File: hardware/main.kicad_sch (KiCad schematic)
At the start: 18 parts, among them J4 ScrewTerminal, J5 ScrewTerminal, J6 ScrewTerminal, K2 ADW11

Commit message: added options
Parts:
- R1, R2: value 3k 100W -> 2k7 50W
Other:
- note added: "Capacitor value: 300 uF Initial charge voltage: 588 V Safety threshold voltage: 60 V Resistance value: 5400 R Safety Voltage achieved by: 3.6975 s Initial power across resistors: 64.0267 W Time constant: 1.62 s Energy discharged to Zero volts: 51.8616 J"
- note removed: "Capacitor value: 300 uF Initial charge voltage: 588 V Safety threshold voltage: 60 V Resistance value: 6000 R Safety Voltage achieved by: 4.10828 s Initial power across resistor: 57.624 W Time constant: 1.8 s Energy discharged to Zero volts: 51.8616 J"

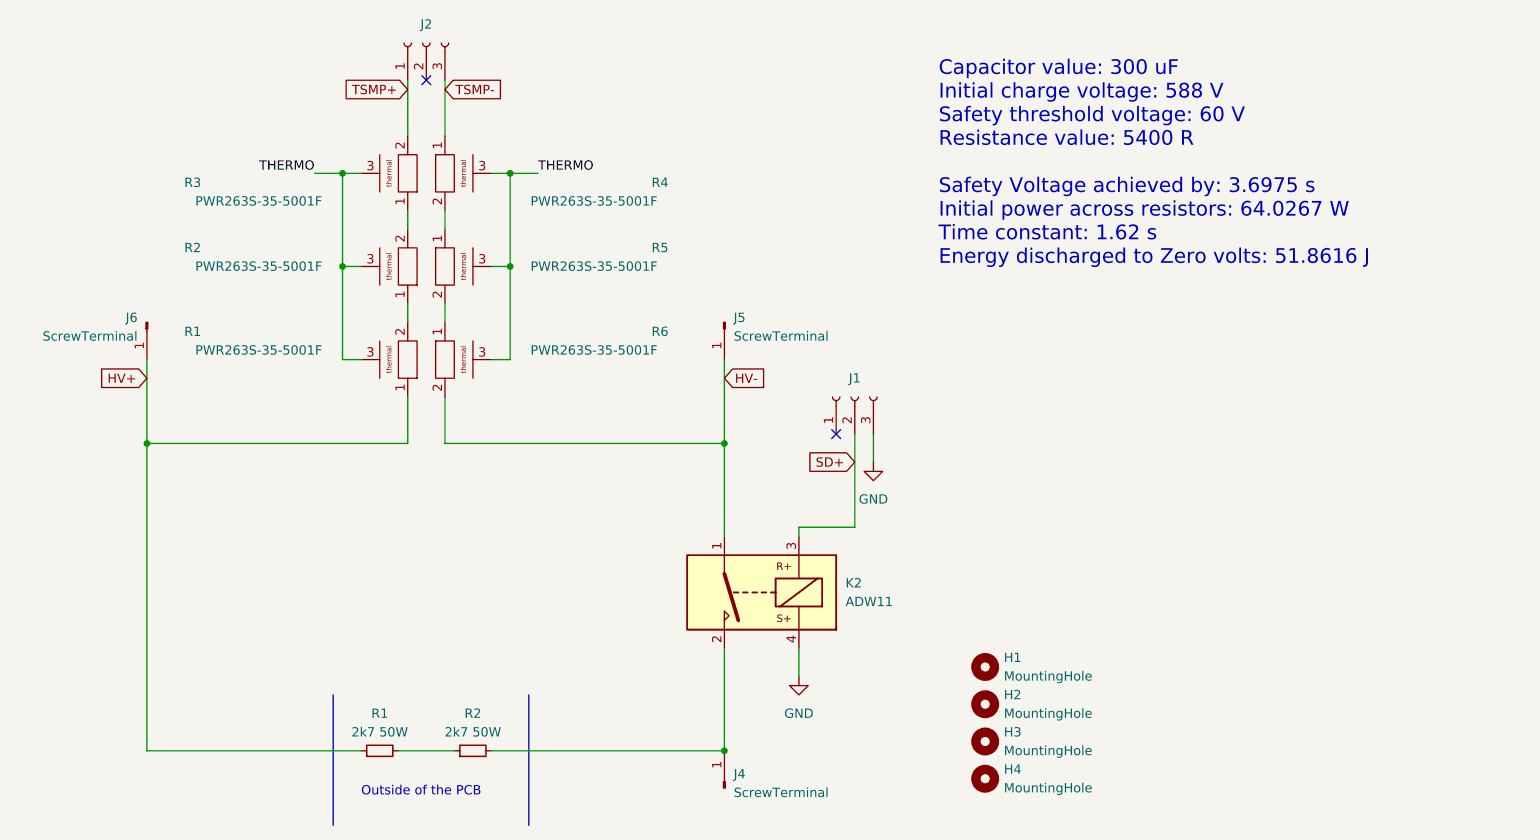
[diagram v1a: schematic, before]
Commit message: Changed resistors to 3x 2k 50W
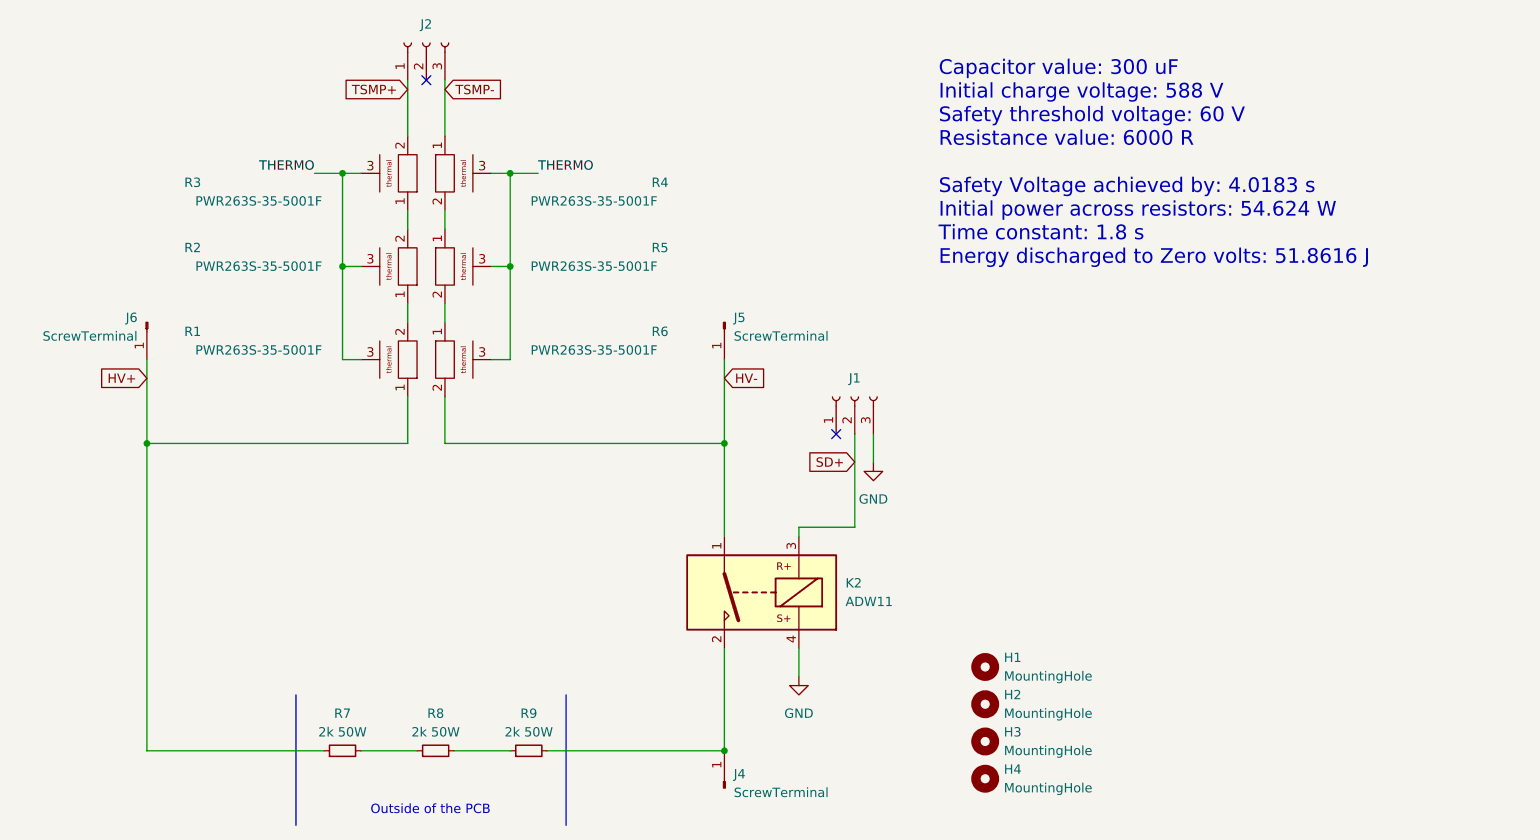
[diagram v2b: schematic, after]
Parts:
- removed R1, R2: 2k7 50W, symbol Device:R_Small
- added R7, R8, R9: 2k 50W, symbol Device:R_Small
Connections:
- net HV+: now also R7.1
- net at J4.1 (Pin_1), K2.2: now also R9.2
- new net: R7.2, R8.1
- new net: R8.2, R9.1
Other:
- note added: "Capacitor value: 300 uF Initial charge voltage: 588 V Safety threshold voltage: 60 V Resistance value: 6000 R Safety Voltage achieved by: 4.0183 s Initial power across resistors: 54.624 W Time constant: 1.8 s Energy discharged to Zero volts: 51.8616 J"
- note removed: "Capacitor value: 300 uF Initial charge voltage: 588 V Safety threshold voltage: 60 V Resistance value: 5400 R Safety Voltage achieved by: 3.6975 s Initial power across resistors: 64.0267 W Time constant: 1.62 s Energy discharged to Zero volts: 51.8616 J"
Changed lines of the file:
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@@
     (stroke (width 0) (type default))
   )
-  (wire (pts (xy 69.85 130.81) (xy 77.47 130.81))
+  (wire (pts (xy 64.77 130.81) (xy 72.39 130.81))
     (stroke (width 0) (type default))
   )
@@
     (stroke (width 0) (type default))
   )
+  (wire (pts (xy 90.17 130.81) (xy 114.3 130.81))
+    (stroke (width 0) (type default))
+  )
   (wire (pts (xy 85.09 77.47) (xy 82.55 77.47))
     (stroke (width 0) (type default))
@@
     (stroke (width 0) (type default))
   )
-  (wire (pts (xy 35.56 130.81) (xy 64.77 130.81))
+  (wire (pts (xy 35.56 130.81) (xy 59.69 130.81))
     (stroke (width 0) (type default))
   )
@@
     (stroke (width 0) (type default))
   )
-  (polyline (pts (xy 87.63 123.19) (xy 87.63 140.97))
+  (polyline (pts (xy 92.71 123.19) (xy 92.71 140.97))
     (stroke (width 0) (type default))
   )
@@
     (stroke (width 0) (type default))
   )
-  (polyline (pts (xy 60.96 123.19) (xy 60.96 140.97))
+  (polyline (pts (xy 55.88 123.19) (xy 55.88 140.97))
     (stroke (width 0) (type default))
   )
@@
     (stroke (width 0) (type default))
   )
-  (wire (pts (xy 82.55 130.81) (xy 114.3 130.81))
+  (wire (pts (xy 77.47 130.81) (xy 85.09 130.81))
     (stroke (width 0) (type default))
   )
@@
     (stroke (width 0) (type default))
   )
-  (text "Outside of the PCB\n" (at 64.77 137.16 0)
+  (text "Outside of the PCB\n" (at 66.04 139.7 0)
     (effects (font (size 1.27 1.27)) (justify left bottom))
   )
-  (text "Capacitor value: 300 uF\nInitial charge voltage: 588 V\nSafety threshold voltage: 60 V\nResistance value: 5400 R\n\nSafety Voltage achieved by: 3.6975 s\nInitial power across resistors: 64.0267 W\nTime constant: 1.62 s\nEnergy discharged to Zero volts: 51.8616 J"
+  (text "Capacitor value: 300 uF\nInitial charge voltage: 588 V\nSafety threshold voltage: 60 V\nResistance value: 6000 R\n\nSafety Voltage achieved by: 4.0183 s\nInitial power across resistors: 54.624 W\nTime constant: 1.8 s\nEnergy discharged to Zero volts: 51.8616 J"
     (at 143.51 64.77 0)
     (effects (font (size 2 2)) (justify left bottom))
@@
     )
   )
+  (symbol (lib_id "Device:R_Small") (at 62.23 130.81 90) (unit 1)
+    (in_bom no) (on_board no) (dnp no) (fields_autoplaced)
+    (property "Reference" "R7" (at 62.23 125.73 90)
+      (effects (font (size 1.27 1.27)))
+    )
+    (property "Value" "2k  50W" (at 62.23 128.27 90)
+      (effects (font (size 1.27 1.27)))
+    )
+    (property "Footprint" "" (at 62.23 130.81 0)
+      (effects (font (size 1.27 1.27)) hide)
+    )
+    (property "Datasheet" "https://media.distrelec.com/Web/Downloads/a_/e1/Arcol_HS10_300_eng_tds.pdf" (at 62.23 130.81 0)
+      (effects (font (size 1.27 1.27)) hide)
+    )
+    (pin "2")
+    (pin "1")
+    (instances
+      (project "main"
+        (path "/b652b05a-4e3d-4ad1-b032-18886abe7d45"
+          (reference "R7") (unit 1)
+        )
+      )
+    )
+  )
   (symbol (lib_id "7696:PWR263S-35-5001F") (at 72.39 62.23 180) (unit 1)
     (in_bom yes) (on_board yes) (dnp no)
@@
     )
   )
-  (symbol (lib_id "Device:R_Small") (at 80.01 130.81 90) (unit 1)
+  (symbol (lib_id "Device:R_Small") (at 87.63 130.81 90) (unit 1)
     (in_bom no) (on_board no) (dnp no) (fields_autoplaced)
-    (property "Reference" "R2" (at 80.01 125.73 90)
-      (effects (font (size 1.27 1.27)))
-    )
-    (property "Value" "2k7  50W" (at 80.01 128.27 90)
-      (effects (font (size 1.27 1.27)))
-    )
-    (property "Footprint" "" (at 80.01 130.81 0)
-      (effects (font (size 1.27 1.27)) hide)
-    )
-    (property "Datasheet" "https://media.distrelec.com/Web/Downloads/a_/e1/Arcol_HS10_300_eng_tds.pdf" (at 80.01 130.81 0)
-      (effects (font (size 1.27 1.27)) hide)
-    )
-    (pin "2")
-    (pin "1")
-    (instances
-      (project "main"
-        (path "/b652b05a-4e3d-4ad1-b032-18886abe7d45"
-          (reference "R2") (unit 1)
+    (property "Reference" "R9" (at 87.63 125.73 90)
+      (effects (font (size 1.27 1.27)))
+    )
+    (property "Value" "2k  50W" (at 87.63 128.27 90)
+      (effects (font (size 1.27 1.27)))
+    )
+    (property "Footprint" "" (at 87.63 130.81 0)
+      (effects (font (size 1.27 1.27)) hide)
+    )
+    (property "Datasheet" "https://media.distrelec.com/Web/Downloads/a_/e1/Arcol_HS10_300_eng_tds.pdf" (at 87.63 130.81 0)
+      (effects (font (size 1.27 1.27)) hide)
+    )
+    (pin "2")
+    (pin "1")
+    (instances
+      (project "main"
+        (path "/b652b05a-4e3d-4ad1-b032-18886abe7d45"
+          (reference "R9") (unit 1)
         )
       )
@@
     )
   )
+  (symbol (lib_id "Device:R_Small") (at 74.93 130.81 90) (unit 1)
+    (in_bom no) (on_board no) (dnp no) (fields_autoplaced)
+    (property "Reference" "R8" (at 74.93 125.73 90)
+      (effects (font (size 1.27 1.27)))
+    )
+    (property "Value" "2k  50W" (at 74.93 128.27 90)
+      (effects (font (size 1.27 1.27)))
+    )
+    (property "Footprint" "" (at 74.93 130.81 0)
+      (effects (font (size 1.27 1.27)) hide)
+    )
+    (property "Datasheet" "https://media.distrelec.com/Web/Downloads/a_/e1/Arcol_HS10_300_eng_tds.pdf" (at 74.93 130.81 0)
+      (effects (font (size 1.27 1.27)) hide)
+    )
+    (pin "2")
+    (pin "1")
+    (instances
+      (project "main"
+        (path "/b652b05a-4e3d-4ad1-b032-18886abe7d45"
+          (reference "R8") (unit 1)
+        )
+      )
+    )
+  )
   (symbol (lib_id "Connector:Conn_01x03_Socket") (at 73.66 34.29 90) (unit 1)
     (in_bom yes) (on_board yes) (dnp no) (fields_autoplaced)
@@
         )
       )
-    )
-  )
-  (symbol (lib_id "Device:R_Small") (at 67.31 130.81 90) (unit 1)
-    (in_bom no) (on_board no) (dnp no) (fields_autoplaced)
-    (property "Reference" "R1" (at 67.31 125.73 90)
-      (effects (font (size 1.27 1.27)))
-    )
-    (property "Value" "2k7  50W" (at 67.31 128.27 90)
-      (effects (font (size 1.27 1.27)))
-    )
-    (property "Footprint" "" (at 67.31 130.81 0)
-      (effects (font (size 1.27 1.27)) hide)
-    )
-    (property "Datasheet" "https://media.distrelec.com/Web/Downloads/a_/e1/Arcol_HS10_300_eng_tds.pdf" (at 67.31 130.81 0)
-      (effects (font (size 1.27 1.27)) hide)
-    )
-    (pin "2")
-    (pin "1")
-    (instances
-      (project "main"
-        (path "/b652b05a-4e3d-4ad1-b032-18886abe7d45"
-          (reference "R1") (unit 1)
-        )
-      )

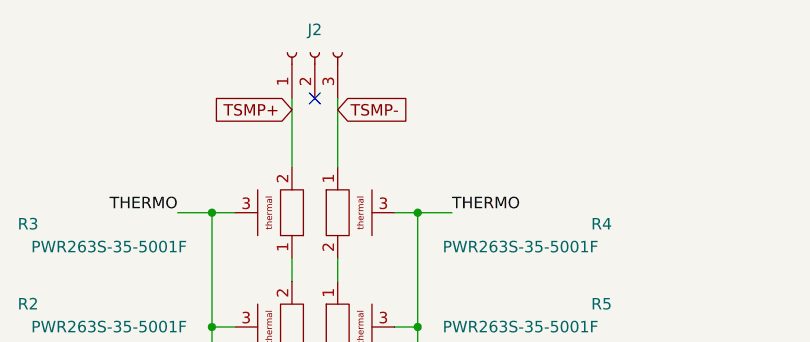
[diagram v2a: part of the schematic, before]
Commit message: Changing the J2 connector
Adapting the connector to the existing harness for PM 09
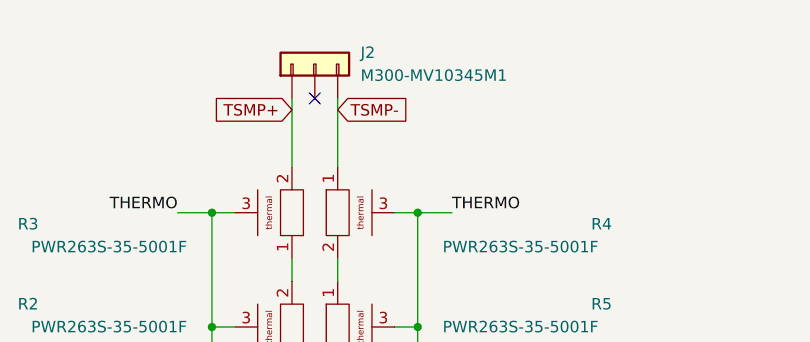
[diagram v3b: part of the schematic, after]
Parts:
- removed J2: ~, d369-g33-xx:D369-G33-XX, symbol Connector:Conn_01x03_Socket
- added J2: M300-MV10345M1, Samacsys:M300MV10345M1, symbol Samacsys_kicad_sym:M300-MV10345M1
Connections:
- net TSMP+: now also J2.1 (Pin_1)
- net TSMP-: now also J2.3 (Pin_3)

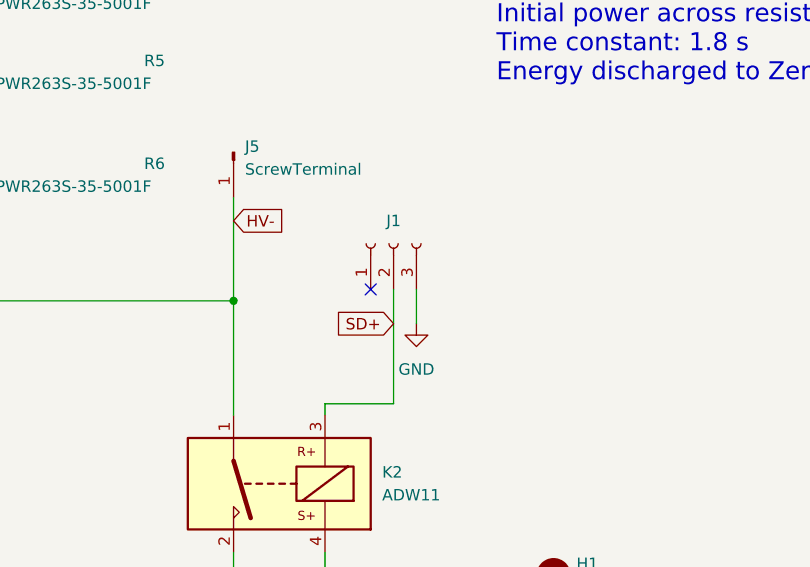
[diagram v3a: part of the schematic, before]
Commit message: Changed the creepage distance between HV and LV, changed thermal refielf for TSMP resistors
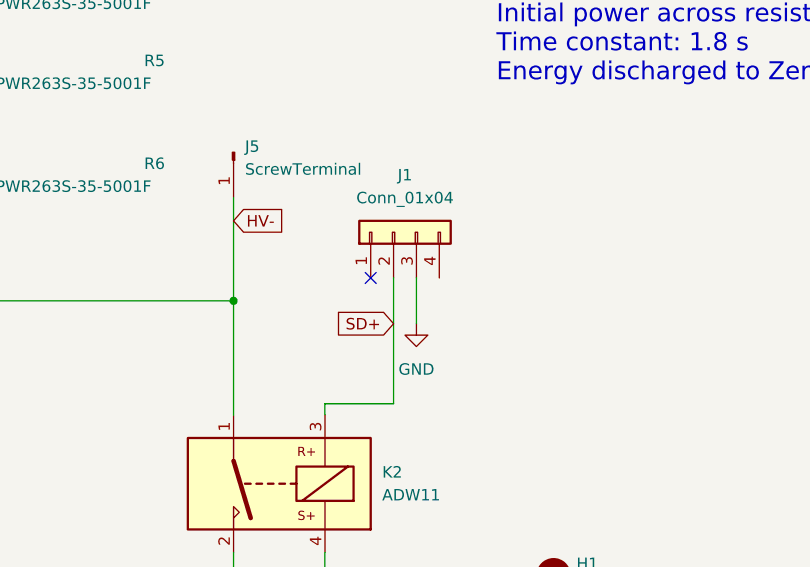
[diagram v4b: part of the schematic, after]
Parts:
- removed J1: ~, d369-g33-xx:D369-G33-XX, symbol Connector:Conn_01x03_Socket
- added J1: Conn_01x04, Harwin_m80:HARWIN_M80-5100442, symbol Connector_Generic:Conn_01x04
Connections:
- net GND: now also J1.3 (Pin_3)
- net SD+: now also J1.2 (Pin_2)
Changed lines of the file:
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@@
 (kicad_sch
-	(version 20231120)
+	(version 20250114)
 	(generator "eeschema")
-	(generator_version "8.0")
+	(generator_version "9.0")
 	(paper "A4")
 	(title_block
@@
 		(comment 1 "Reviewer:")
 	)
+	(text "Outside of the PCB\n"
+		(exclude_from_sim no)
+		(at 66.04 139.7 0)
+		(effects
+			(font
+				(size 1.27 1.27)
+			)
+			(justify left bottom)
+		)
+	)
+	(text "Capacitor value: 300 uF\nInitial charge voltage: 588 V\nSafety threshold voltage: 60 V\nResistance value: 6000 R\n\nSafety Voltage achieved by: 4.0183 s\nInitial power across resistors: 54.624 W\nTime constant: 1.8 s\nEnergy discharged to Zero volts: 51.8616 J"
+		(exclude_from_sim no)
+		(at 143.51 64.77 0)
+		(effects
+			(font
+				(size 2 2)
+			)
+			(justify left bottom)
+		)
+	)
 	(junction
 		(at 35.56 88.9)
@@
 	)
 	(no_connect
-		(at 129.54 87.63)
+		(at 129.54 86.36)
 	)
 	(wire
@@
 	(wire
 		(pts
-			(xy 134.62 87.63) (xy 134.62 91.44)
+			(xy 134.62 86.36) (xy 134.62 91.44)
 		)
 		(stroke
@@
 	(wire
 		(pts
-			(xy 132.08 87.63) (xy 132.08 100.33)
+			(xy 132.08 86.36) (xy 132.08 100.33)
 		)
 		(stroke
@@
 		)
 	)
-	(text "Outside of the PCB\n"
-		(exclude_from_sim no)
-		(at 66.04 139.7 0)
+	(label "THERMO"
+		(at 58.42 52.07 180)
 		(effects
 			(font
 				(size 1.27 1.27)
 			)
-			(justify left bottom)
-		)
-	)
-	(text "Capacitor value: 300 uF\nInitial charge voltage: 588 V\nSafety threshold voltage: 60 V\nResistance value: 6000 R\n\nSafety Voltage achieved by: 4.0183 s\nInitial power across resistors: 54.624 W\nTime constant: 1.8 s\nEnergy discharged to Zero volts: 51.8616 J"
-		(exclude_from_sim no)
-		(at 143.51 64.77 0)
-		(effects
-			(font
-				(size 2 2)
-			)
-			(justify left bottom)
-		)
-	)
-	(label "THERMO"
-		(at 58.42 52.07 180)
-		(fields_autoplaced yes)
-		(effects
-			(font
-				(size 1.27 1.27)
-			)
 			(justify right bottom)
 		)
@@
 	(label "THERMO"
 		(at 88.9 52.07 0)
-		(fields_autoplaced yes)
 		(effects
 			(font
@@
 	)
 	(symbol
-		(lib_id "Connector:Conn_01x03_Socket")
-		(at 132.08 82.55 90)
-		(unit 1)
-		(exclude_from_sim no)
-		(in_bom yes)
-		(on_board yes)
-		(dnp no)
-		(fields_autoplaced yes)
-		(property "Reference" "J1"
-			(at 132.08 80.01 90)
-			(effects
-				(font
-					(size 1.27 1.27)
-				)
-			)
-		)
-		(property "Value" "~"
-			(at 132.08 80.01 90)
-			(effects
-				(font
-					(size 1.27 1.27)
-				)
-			)
-		)
-		(property "Footprint" "d369-g33-xx:D369-G33-XX"
-			(at 132.08 82.55 0)
-			(effects
-				(font
-					(size 1.27 1.27)
-				)
-				(hide yes)
-			)
-		)
-		(property "Datasheet" "~"
-			(at 132.08 82.55 0)
-			(effects
-				(font
-					(size 1.27 1.27)
-				)
-				(hide yes)
-			)
-		)
-		(property "Description" ""
-			(at 132.08 82.55 0)
-			(effects
-				(font
-					(size 1.27 1.27)
-				)
-				(hide yes)
-			)
-		)
-		(pin "3"
-		)
-		(pin "1"
-		)
-		(pin "2"
-		)
-		(instances
-			(project "main"
-				(path "/b652b05a-4e3d-4ad1-b032-18886abe7d45"
-					(reference "J1")
-					(unit 1)
-				)
-			)
-		)
-	)
-	(symbol
 		(lib_id "Mechanical:MountingHole")
 		(at 149.86 134.62 0)
@@
 	)
 	(symbol
+		(lib_id "Connector_Generic:Conn_01x04")
+		(at 132.08 81.28 90)
+		(unit 1)
+		(exclude_from_sim no)
+		(in_bom yes)
+		(on_board yes)
+		(dnp no)
+		(fields_autoplaced yes)
+		(property "Reference" "J1"
+			(at 133.35 74.93 90)
+			(effects
+				(font
+					(size 1.27 1.27)
+				)
+			)
+		)
+		(property "Value" "Conn_01x04"
+			(at 133.35 77.47 90)
+			(effects
+				(font
+					(size 1.27 1.27)
+				)
+			)
+		)
+		(property "Footprint" "Harwin_m80:HARWIN_M80-5100442"
+			(at 132.08 81.28 0)
+			(effects
+				(font
+					(size 1.27 1.27)
+				)
+				(hide yes)
+			)
+		)
+		(property "Datasheet" "~"
+			(at 132.08 81.28 0)
+			(effects
+				(font
+					(size 1.27 1.27)
+				)
+				(hide yes)
+			)
+		)
+		(property "Description" "Generic connector, single row, 01x04, script generated (kicad-library-utils/schlib/autogen/connector/)"
+			(at 132.08 81.28 0)
+			(effects
+				(font
+					(size 1.27 1.27)
+				)
+				(hide yes)
+			)
+		)
+		(pin "4"
+		)
+		(pin "1"
+		)
+		(pin "3"
+		)
+		(pin "2"
+		)
+		(instances
+			(project ""
+				(path "/b652b05a-4e3d-4ad1-b032-18886abe7d45"
+					(reference "J1")
+					(unit 1)
+				)
+			)
+		)
+	)
+	(symbol
 		(lib_id "Mechanical:MountingHole")
 		(at 149.86 124.46 0)
@@
 		)
 	)
+	(embedded_fonts no)
 )
